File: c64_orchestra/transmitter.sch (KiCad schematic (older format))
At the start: 13 parts

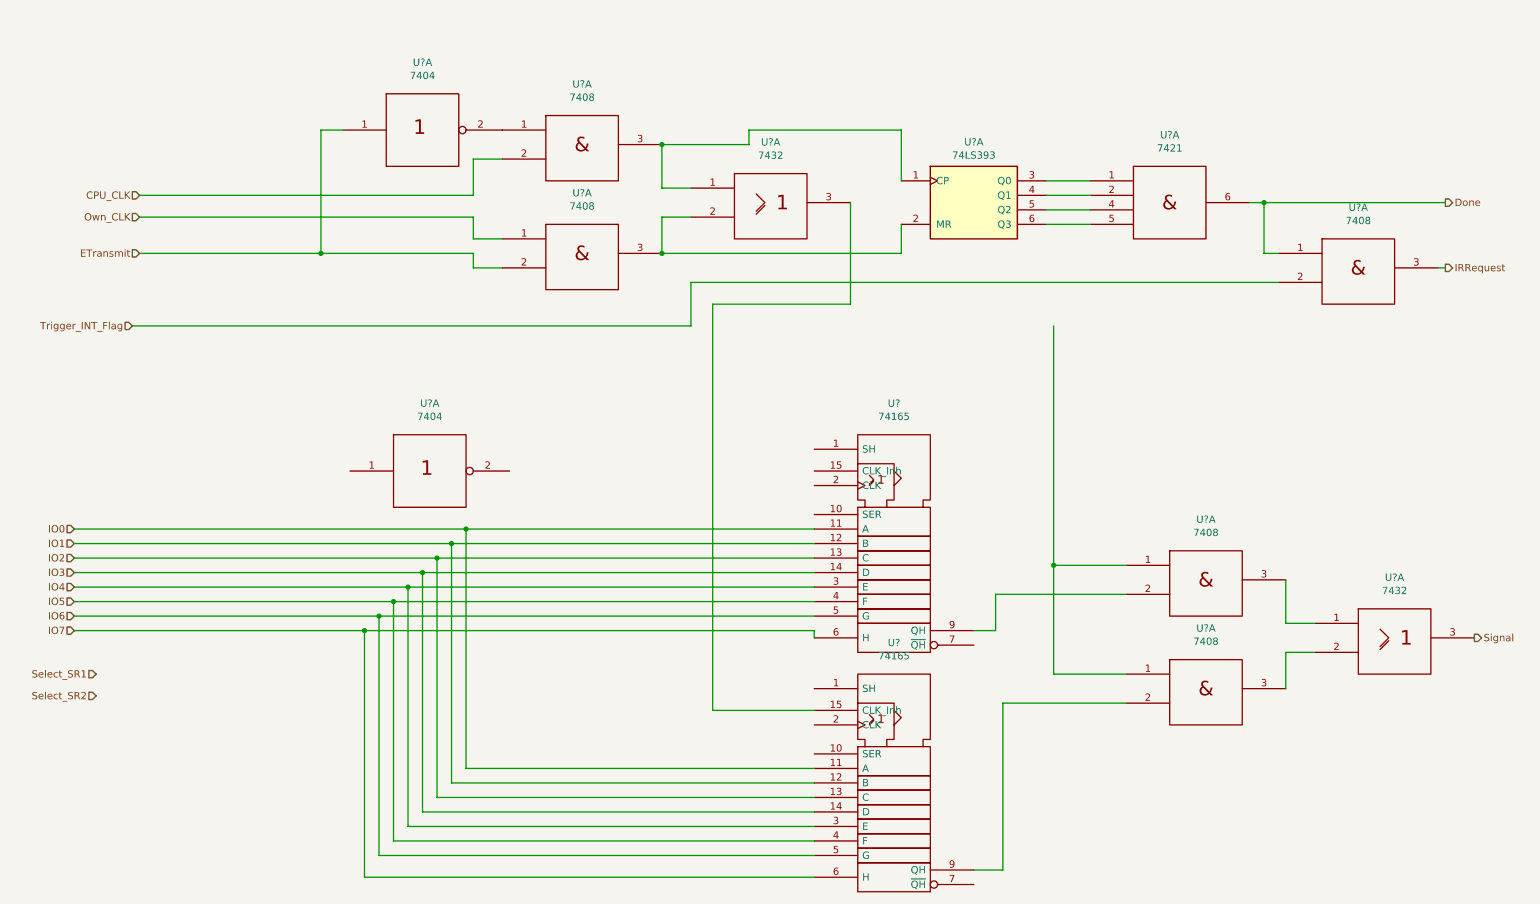
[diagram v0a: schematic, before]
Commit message: Added parts of schematic and worked on pcb layout.
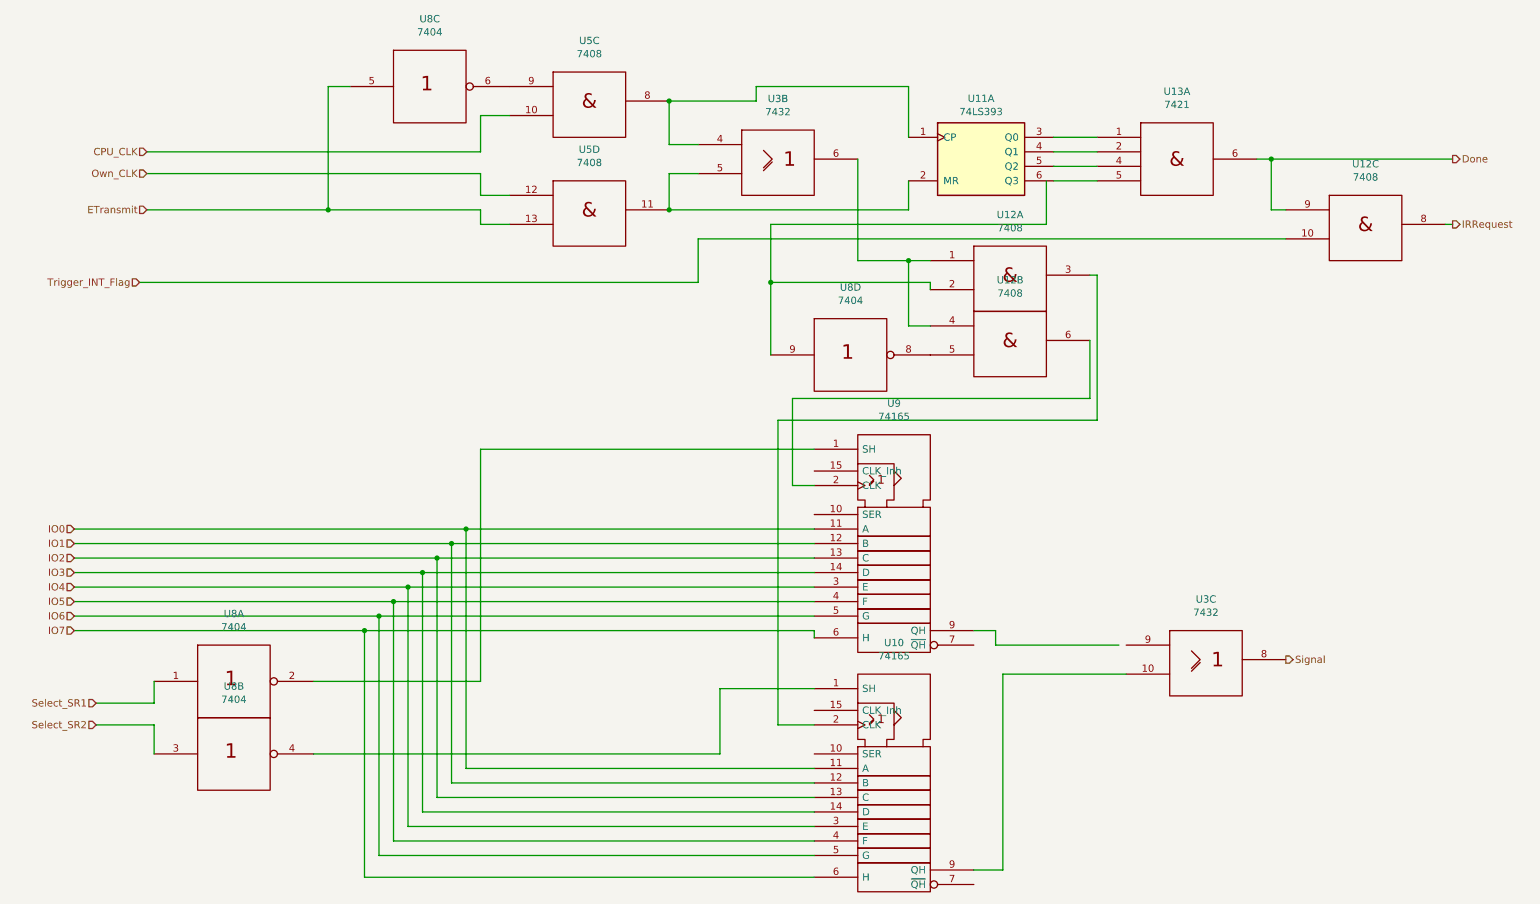
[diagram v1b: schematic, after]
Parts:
- removed U? (x2): 7408, symbol 74xx_IEEE:7408
- removed U?: 7404, symbol 74xx_IEEE:7404
- added unit 1 of U12
- added unit 2 of U12
- added unit 1 of U8
- added unit 2 of U8
- added unit 4 of U8
- U10, U11, U9: renamed from U?; footprint (none) -> Package_DIP:DIP-16_W7.62mm
- U12, U13, U3, U5: renamed from U?; footprint (none) -> Package_DIP:DIP-14_W7.62mm
- U8: renamed from U?; footprint (none) -> Package_DIP:DIP-12_W10.16mm
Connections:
- net Vcc is gone; now on net Gnd: U12.14 (Vcc), U13.14 (Vcc), U3.14 (Vcc), U3.14 (Vcc), U5.14 (Vcc), U5.14 (Vcc), U8.14 (Vcc)
- net CPU_CLK: now also U5.10; no longer U5.2
- net Done: now also U12.9; no longer U12.1
- net ETransmit: now also U5.13, U8.5; no longer U5.2, U8.1
- net Gnd: now also U12.14 (Vcc), U12.14 (Vcc), U12.7 (Gnd), U12.7 (Gnd), U8.14 (Vcc), U8.14 (Vcc), U8.14 (Vcc), U8.7 (Gnd), U8.7 (Gnd), U8.7 (Gnd)
- net IRRequest: now also U12.8; no longer U12.3
- net Own_CLK: now also U5.12; no longer U5.1
- net Select_SR1: now also U8.1
- net Select_SR2: now also U8.3
- net Signal: now also U3.8; no longer U3.3
- net Trigger_INT_Flag: now also U12.10; no longer U12.2
- net at U10.15 (CLK_Inh): no longer U3.3
- net at U10.9 (QH): now also U3.10
- net at U9.1 (SH): now also U8.2
- net at U9.2 (CLK): now also U12.6
- net at U10.1 (SH): now also U8.4
- net at U10.2 (CLK): now also U12.3
- new net: U11.1 (CP), U3.4, U5.8
- new net: U5.9, U8.6
- new net: U11.2 (MR), U3.5, U5.11
- new net: U12.1, U12.4, U3.6
- new net: U12.2, U8.9
- new net: U12.5, U8.8
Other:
- moved on the sheet: U11A, U13A

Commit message: Changed the logic gates' numbering, changed some gates for todos.
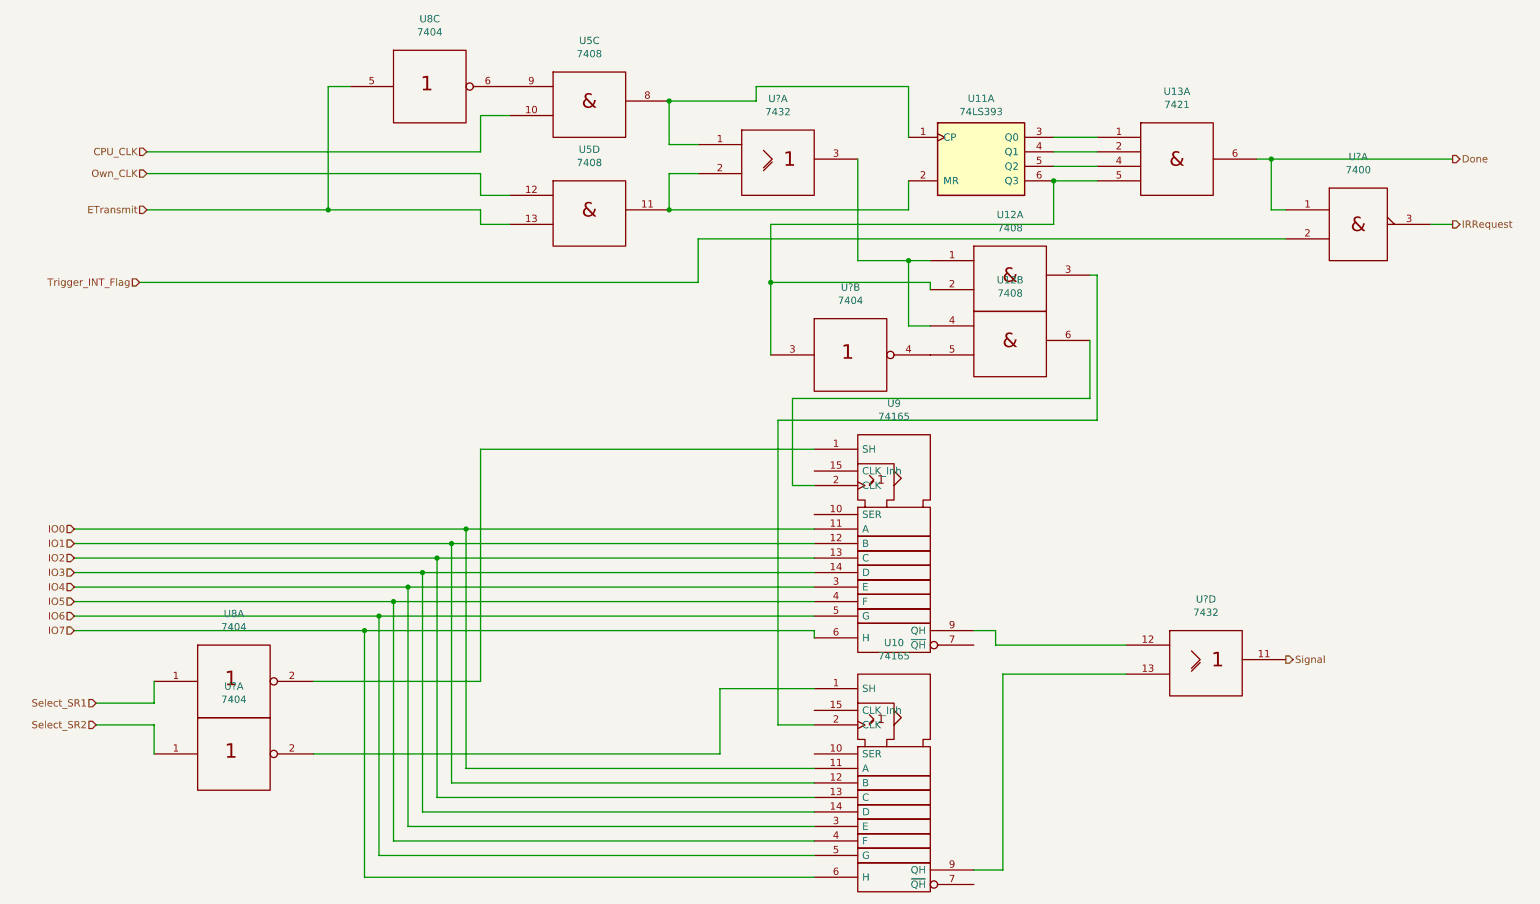
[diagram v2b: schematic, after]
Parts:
- removed unit 3 of U12
- removed U3: 7432, Package_DIP:DIP-14_W7.62mm, symbol 74xx_IEEE:7432
- removed unit 2 of U8
- removed unit 4 of U8
- added U?: 7400, symbol 74xx_IEEE:7400
- added U? (x2): 7432, symbol 74xx_IEEE:7432
- added U? (x2): 7404, symbol 74xx_IEEE:7404
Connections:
- net Done: now also U?.1
- net GND: now also U?.7 (GND)
- net Gnd: now also U?.14 (Vcc), U?.14 (Vcc), U?.14 (Vcc), U?.14 (Vcc), U?.14 (Vcc), U?.7 (Gnd), U?.7 (Gnd), U?.7 (Gnd), U?.7 (Gnd)
- net IRRequest: now also U?.3
- net Select_SR2: now also U?.1
- net Signal: now also U?.11
- net Trigger_INT_Flag: now also U?.2
- net at U11.1 (CP), U5.8: now also U?.1
- net at U11.2 (MR), U5.11: now also U?.2
- net at U12.1, U12.4: now also U?.3
- net at U10.9 (QH): now also U?.13
- net at U11.6 (Q3), U13.5: now also U12.2, U?.3
- net at U10.1 (SH): now also U?.2
- net at U9.9 (QH): now also U?.12
- net at U12.5: now also U?.4
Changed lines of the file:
@@
 	9100 1250 9100 1600
-Wire Wire Line
-	10300 1700 10350 1700
-$Comp
-L 74xx_IEEE:7408 U12
-U 3 1 5F8D99F8
-P 9750 1700
-F 0 "U12" H 9750 2116 50  0000 C CNN
-F 1 "7408" H 9750 2025 50  0000 C CNN
-F 2 "Package_DIP:DIP-14_W7.62mm" H 9750 1700 50  0001 C CNN
-F 3 "" H 9750 1700 50  0001 C CNN
-	3    9750 1700
-	1    0    0    -1
-$EndComp
 Wire Wire Line
 	9000 1250 9100 1250
@@
 	1    0    0    -1
 $EndComp
-$Comp
-L 74xx_IEEE:7432 U3
-U 3 1 5F8AB588
-P 8650 4700
-F 0 "U3" H 8650 5116 50  0000 C CNN
-F 1 "7432" H 8650 5025 50  0000 C CNN
-F 2 "Package_DIP:DIP-14_W7.62mm" H 8650 4700 50  0001 C CNN
-F 3 "" H 8650 4700 50  0001 C CNN
-	3    8650 4700
-	1    0    0    -1
-$EndComp
 Connection ~ 2600 1600
 Wire Wire Line
@@
 Wire Wire Line
 	4950 850  4950 1150
-$Comp
-L 74xx_IEEE:7432 U3
-U 2 1 5F89A86E
-P 5700 1250
-F 0 "U3" H 5700 1666 50  0000 C CNN
-F 1 "7432" H 5700 1575 50  0000 C CNN
-F 2 "Package_DIP:DIP-14_W7.62mm" H 5700 1250 50  0001 C CNN
-F 3 "" H 5700 1250 50  0001 C CNN
-	2    5700 1250
-	1    0    0    -1
-$EndComp
 $Comp
 L 74xx_IEEE:7408 U5
@@
 CPU_CLK
 Wire Wire Line
-	7600 1400 7900 1400
-Wire Wire Line
 	1350 1200 3650 1200
 Wire Wire Line
@@
 	7250 4800 7250 6150
 Wire Wire Line
-	8050 4600 7200 4600
-Wire Wire Line
 	7200 4600 7200 4500
 $Comp
@@
 	1    0    0    -1
 $EndComp
-$Comp
-L 74xx_IEEE:7404 U8
-U 2 1 5F8DF2B9
-P 1950 5350
-F 0 "U8" H 1950 5816 50  0000 C CNN
-F 1 "7404" H 1950 5725 50  0000 C CNN
-F 2 "Package_DIP:DIP-12_W10.16mm" H 1950 5350 50  0001 C CNN
-F 3 "" H 1950 5350 50  0001 C CNN
-	2    1950 5350
-	1    0    0    -1
-$EndComp
 Wire Wire Line
 	1000 5000 1400 5000
@@
 	1    0    0    -1
 $EndComp
-$Comp
-L 74xx_IEEE:7404 U8
-U 4 1 5F90AD88
-P 6200 2600
-F 0 "U8" H 6200 3066 50  0000 C CNN
-F 1 "7404" H 6200 2975 50  0000 C CNN
-F 2 "Package_DIP:DIP-12_W10.16mm" H 6200 2600 50  0001 C CNN
-F 3 "" H 6200 2600 50  0001 C CNN
-	4    6200 2600
-	1    0    0    -1
-$EndComp
-Wire Wire Line
-	7550 1400 7550 1700
-Wire Wire Line
-	7550 1700 5650 1700
 Wire Wire Line
 	5650 1700 5650 2100
@@
 Wire Wire Line
 	5700 5150 5950 5150
+$Comp
+L 74xx_IEEE:7400 U?
+U 1 1 5F8F600F
+P 9700 1700
+F 0 "U?" H 9700 2166 50  0000 C CNN
+F 1 "7400" H 9700 2075 50  0000 C CNN
+F 2 "" H 9700 1700 50  0001 C CNN
+F 3 "" H 9700 1700 50  0001 C CNN
+	1    9700 1700
+	1    0    0    -1
+$EndComp
+Wire Wire Line
+	10200 1700 10350 1700
+Wire Wire Line
+	7200 4600 8100 4600
+Wire Wire Line
+	7900 1400 7600 1400
+Wire Wire Line
+	7600 1700 7600 1400
+Wire Wire Line
+	5650 1700 7600 1700
+Connection ~ 7600 1400
+$Comp
+L 74xx_IEEE:7432 U?
+U 4 1 5F95A17C
+P 8650 4700
+F 0 "U?" H 8650 5116 50  0000 C CNN
+F 1 "7432" H 8650 5025 50  0000 C CNN
+F 2 "" H 8650 4700 50  0001 C CNN
+F 3 "" H 8650 4700 50  0001 C CNN
+	4    8650 4700
+	1    0    0    -1
+$EndComp
+$Comp
+L 74xx_IEEE:7432 U?
+U 1 1 5F962F60
+P 5700 1250
+F 0 "U?" H 5700 1666 50  0000 C CNN
+F 1 "7432" H 5700 1575 50  0000 C CNN
+F 2 "" H 5700 1250 50  0001 C CNN
+F 3 "" H 5700 1250 50  0001 C CNN
+	1    5700 1250
+	1    0    0    -1
+$EndComp
+$Comp
+L 74xx_IEEE:7404 U?
+U 2 1 5F981E75
+P 6200 2600
+F 0 "U?" H 6200 3066 50  0000 C CNN
+F 1 "7404" H 6200 2975 50  0000 C CNN
+F 2 "" H 6200 2600 50  0001 C CNN
+F 3 "" H 6200 2600 50  0001 C CNN
+	2    6200 2600
+	1    0    0    -1
+$EndComp
+$Comp
+L 74xx_IEEE:7404 U?
+U 1 1 5F98AB49
+P 1950 5350
+F 0 "U?" H 1950 5816 50  0000 C CNN
+F 1 "7404" H 1950 5725 50  0000 C CNN
+F 2 "" H 1950 5350 50  0001 C CNN
+F 3 "" H 1950 5350 50  0001 C CNN
+	1    1950 5350
+	1    0    0    -1
+$EndComp
 $EndSCHEMATC
